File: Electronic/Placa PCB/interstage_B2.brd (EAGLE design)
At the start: 82.5 x 29 mm, 6 parts, among them J1 0532611271, Q1 PMV16XNR, U1 LM70CIMM-3, U2 LM70CIMM-3

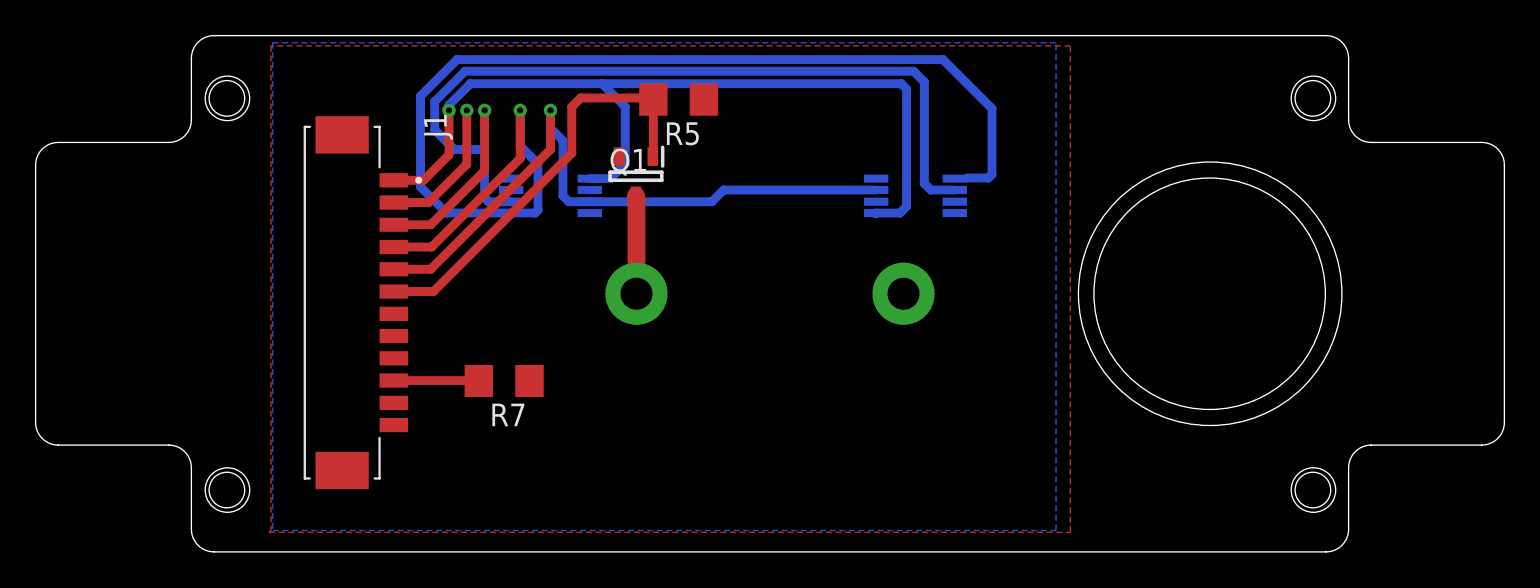
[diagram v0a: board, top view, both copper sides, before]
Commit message: Ensamblaje placa
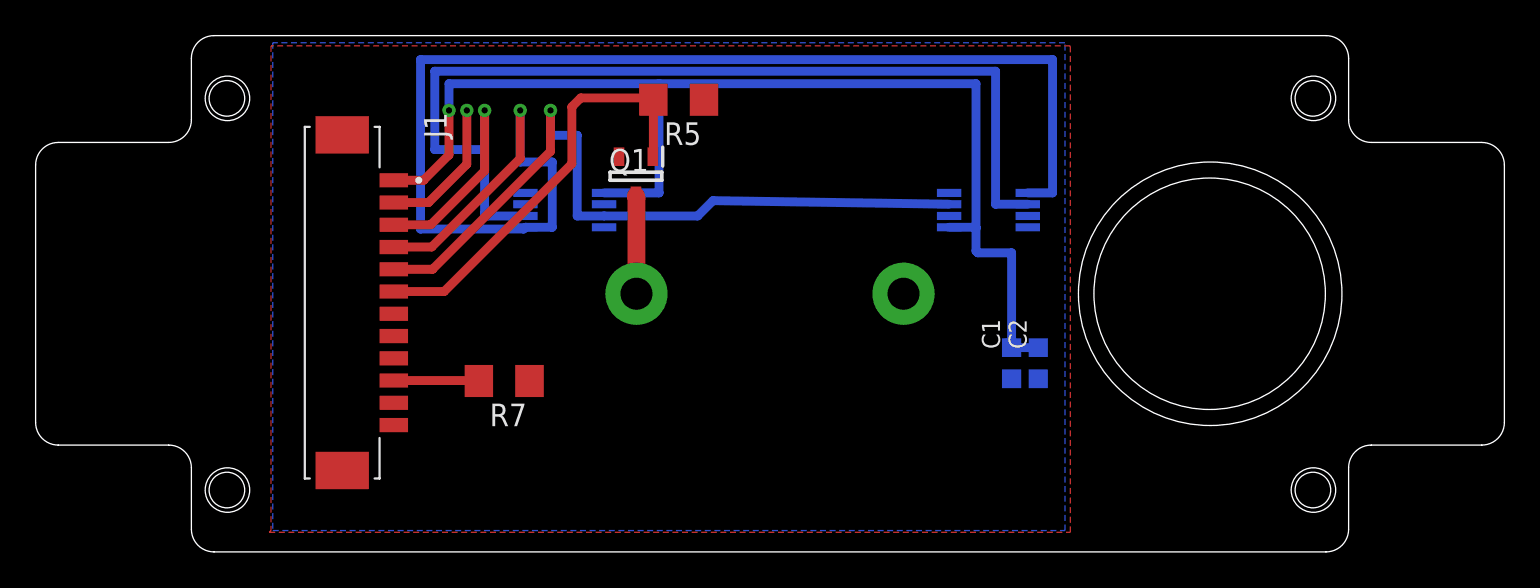
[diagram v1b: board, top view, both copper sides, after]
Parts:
- added C1, C2: 0.1pF, rcl:C0603K
- moved U1 4.18 mm to (44.8, 19.2)
- moved U2 1.13 mm to (21.0, 19.2)
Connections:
- net GND: now also C1.2, C2.2
- net VCC: now also C1.1, C2.1
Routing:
- net VCC: track 48.7 -> 66.8 mm
- net MISO: track 69.5 -> 81.6 mm
- net SCK: track 57.1 -> 65.4 mm
- net MOSI: track 36.9 -> 42.5 mm
